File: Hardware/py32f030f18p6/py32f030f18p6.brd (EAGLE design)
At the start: 43.9 x 18.6 mm, 29 parts, among them IC2 AP2114HA-3.3TRG1, J1 USB_MINI-B_SMT, Y1 DSC6083CI1A-350K000T

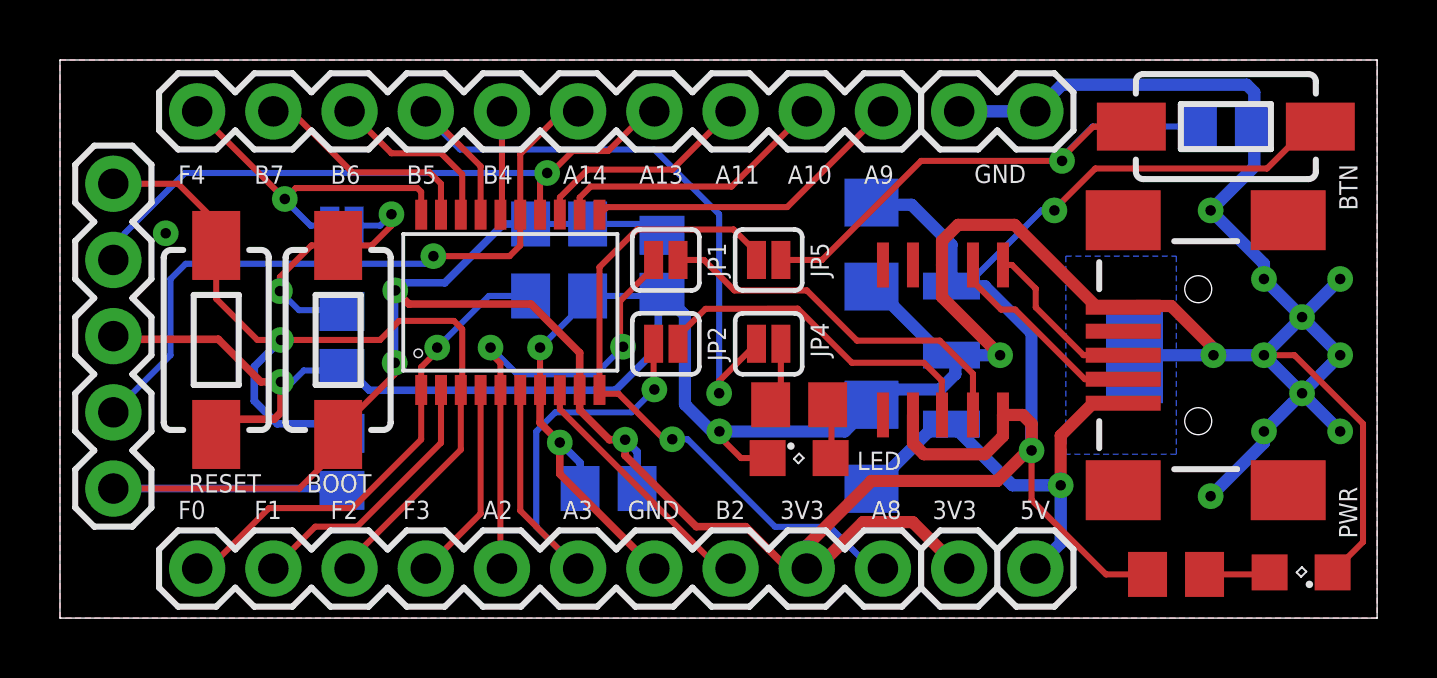
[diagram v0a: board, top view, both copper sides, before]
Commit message: Remove button replace with header, removed reset pin
Replaced the boot button with a header, removed reset pin
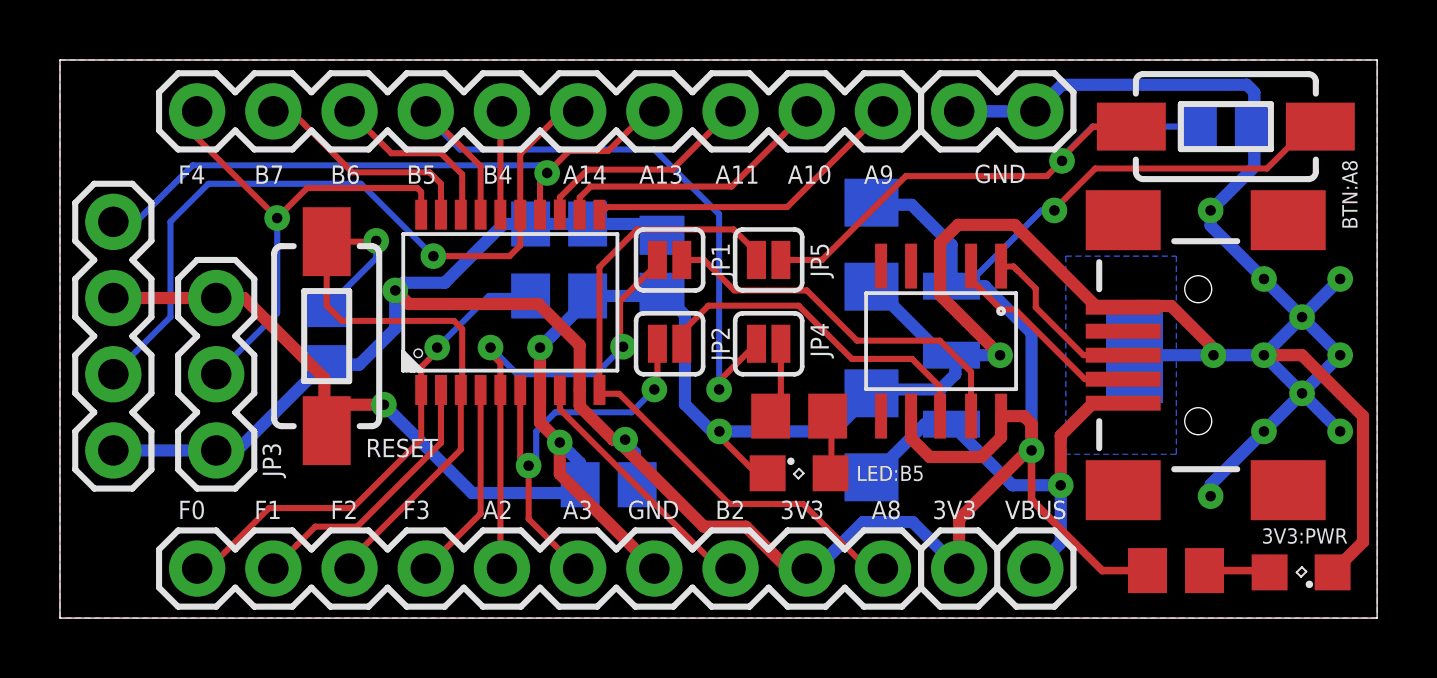
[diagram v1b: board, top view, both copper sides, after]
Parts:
- removed J2: (no value), SparkFun-Connectors:1X05
- removed LED: 20ma, led:SML0805
- removed R5: (no value), rcl:R0805
- removed S3: RESET, SparkFun-Switches:TACTILE_SWITCH_SMD_6.0X3.5MM
- added J7: (no value), SparkFun-Connectors:1X04
- added L1: 20ma, led:SML0805
- JP3: value JUMPER-SMT_2_NC_PASTE_SILK -> 455-1750-1-ND; device SparkFun-Jumpers:SMT-JUMPER_2_NC_PASTE_SILK -> SparkFun-Connectors:1X03
- R1, R2: value (none) -> 10K
- U$1: device ch340k-nopad:ESSOP-10 -> angelo-ch340k-nopad:ESSOP-10
- moved JP3 8.59 mm to (5.21, 5.59), flipped to the top, turned to 90 degrees
- moved R1 4.22 mm to (8.89, 9.40)
- moved S1 3.69 mm to (8.89, 9.40)
- moved C10 0.38 mm to (27.1, 6.09)
- moved R3 0.38 mm to (24.6, 6.73)
- moved C1 0.13 mm to (18.3, 4.45)
- moved R4 0.13 mm to (37.2, 1.58)
- moved JP1 0.13 mm to (20.3, 11.9)
- moved JP2 0.13 mm to (20.3, 9.14)
- moved U$1 0.07 mm to (29.4, 9.23)
- renumbered PWR to L2
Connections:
- removed net N$1: JP3.2, R5.2, S3.1
- net +3V3: now also J7.4, JP3.1; no longer J2.5, S3.2
- net GND: now also J7.2, JP3.3, L1.C; no longer J2.3, LED.C, R5.1
- net N$2: now also L1.A; no longer LED.A
- net PA13-SWDIO: now also J7.1; no longer J2.2
- net PA14-SWCLK: now also J7.3; no longer J2.4
- net PF2-NRST: no longer J2.1
- net PF4-BOOT0: now also JP3.2; no longer JP3.1
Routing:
- net +3V3: track 108.4 -> 94.1 mm, vias 5 -> 4
- net PF2-NRST: track 31.0 -> 21.1 mm
- net N$1: track 9.03 -> 0.00 mm, vias 2 -> 0
- net PF4-BOOT0: track 11.5 -> 16.7 mm
- net GND: track 128.5 -> 123.8 mm, vias 17 -> 16
- net PA3-U1RX: track 18.0 -> 14.1 mm, vias 1 -> 2
- net PA14-SWCLK: track 22.9 -> 24.8 mm
- net PA13-SWDIO: track 21.9 -> 21.3 mm
- net PA8: track 22.4 -> 22.3 mm, vias 1 -> 0
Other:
- board text added: "3V3:PWR"
- board text added: "BTN:A8"
- board text added: "JP3"
- board text added: "LED:B5"
- board text added: "RX:A3"
- board text added: "SWC: A14"
- board text added: "SWD: A13"
- board text added: "TX:A2"
- board text added: "VBUS"
- board text removed: "5V"
- board text removed: "BTN"
- board text removed: "RST"

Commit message: Added missing pullup on RX to fix bootloader issue, updated the firmware so it outputs message on uart
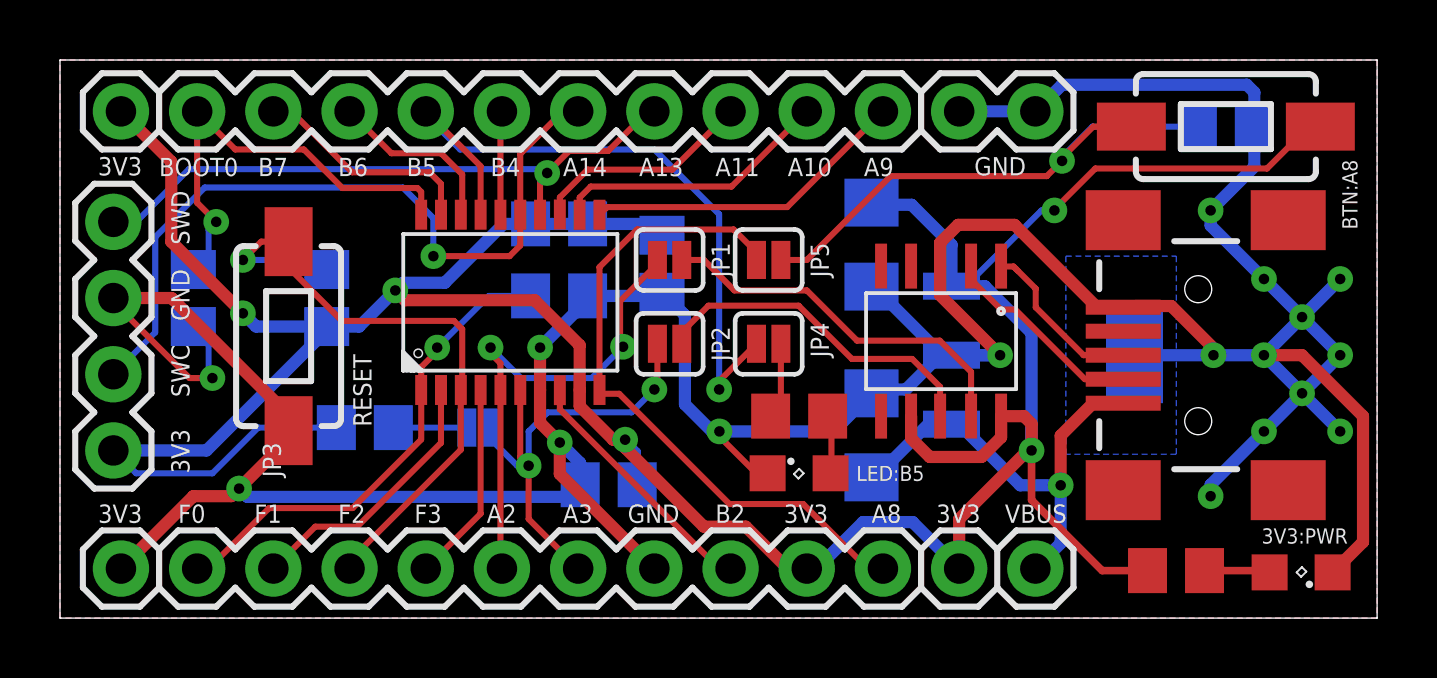
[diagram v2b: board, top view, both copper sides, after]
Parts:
- removed JP3: 455-1750-1-ND, SparkFun-Connectors:1X03
- added J2, J8: (no value), SparkFun-Connectors:1X01
- added JP6: JUMPER-SMT_2_NC_PASTE_SILK, SparkFun-Jumpers:SMT-JUMPER_2_NC_PASTE_SILK
- added R5: 1.8k, rcl:R0805
- added R6: 10K, rcl:R0805
- moved S1 1.27 mm to (7.62, 9.40)
- moved R1 1.27 mm to (8.89, 10.7)
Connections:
- new net N$1: JP6.2, R5.1
- net +3V3: now also J2.1, R5.2; no longer JP3.1
- net GND: now also J8.1, R6.1; no longer JP3.3
- net PA3-U1RX: now also JP6.1
- net PF4-BOOT0: now also R6.2; no longer JP3.2
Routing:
- net +3V3: track 94.1 -> 113.2 mm, vias 4 -> 5
- net GND: track 123.8 -> 138.7 mm, vias 16 -> 17
- net N$1: track 0.00 -> 2.45 mm
- net PA3-U1RX: track 14.1 -> 16.2 mm
- net PF4-BOOT0: track 16.7 -> 15.2 mm
- net PF2-NRST: track 21.1 -> 21.7 mm
- net PA14-SWCLK: track 24.8 -> 25.4 mm
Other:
- board text added: "BOOT0"
- board text added: "PYBUG32-30 RevB"
- board text removed: "BOOT"
- board text removed: "F4"
- board text removed: "PYBUG32-30 RevA"
